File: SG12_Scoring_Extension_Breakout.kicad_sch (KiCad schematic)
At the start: 14 parts, among them J1 RJ45, J2 Barrel_Jack_MountingPin, J3 Barrel_Jack_MountingPin, J4 Barrel_Jack_MountingPin, J5 Barrel_Jack_MountingPin, J6 Barrel_Jack_MountingPin, Q1 IRF4905, Q2 IRF4905, Q3 IRF4905, Q4 IRF4905

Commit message: Messed up a footprint
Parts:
- R4: footprint Connector_RJ:RJ45_Amphenol_54602-x08_Horizontal -> Resistor_THT:R_Axial_DIN0207_L6.3mm_D2.5mm_P10.16mm_Horizontal
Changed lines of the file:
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@@
       (effects (font (size 1.27 1.27)) (justify left))
     )
-    (property "Footprint" "Connector_RJ:RJ45_Amphenol_54602-x08_Horizontal" (at 115.062 157.48 90)
+    (property "Footprint" "Resistor_THT:R_Axial_DIN0207_L6.3mm_D2.5mm_P10.16mm_Horizontal" (at 115.062 157.48 90)
       (effects (font (size 1.27 1.27)) hide)
     )

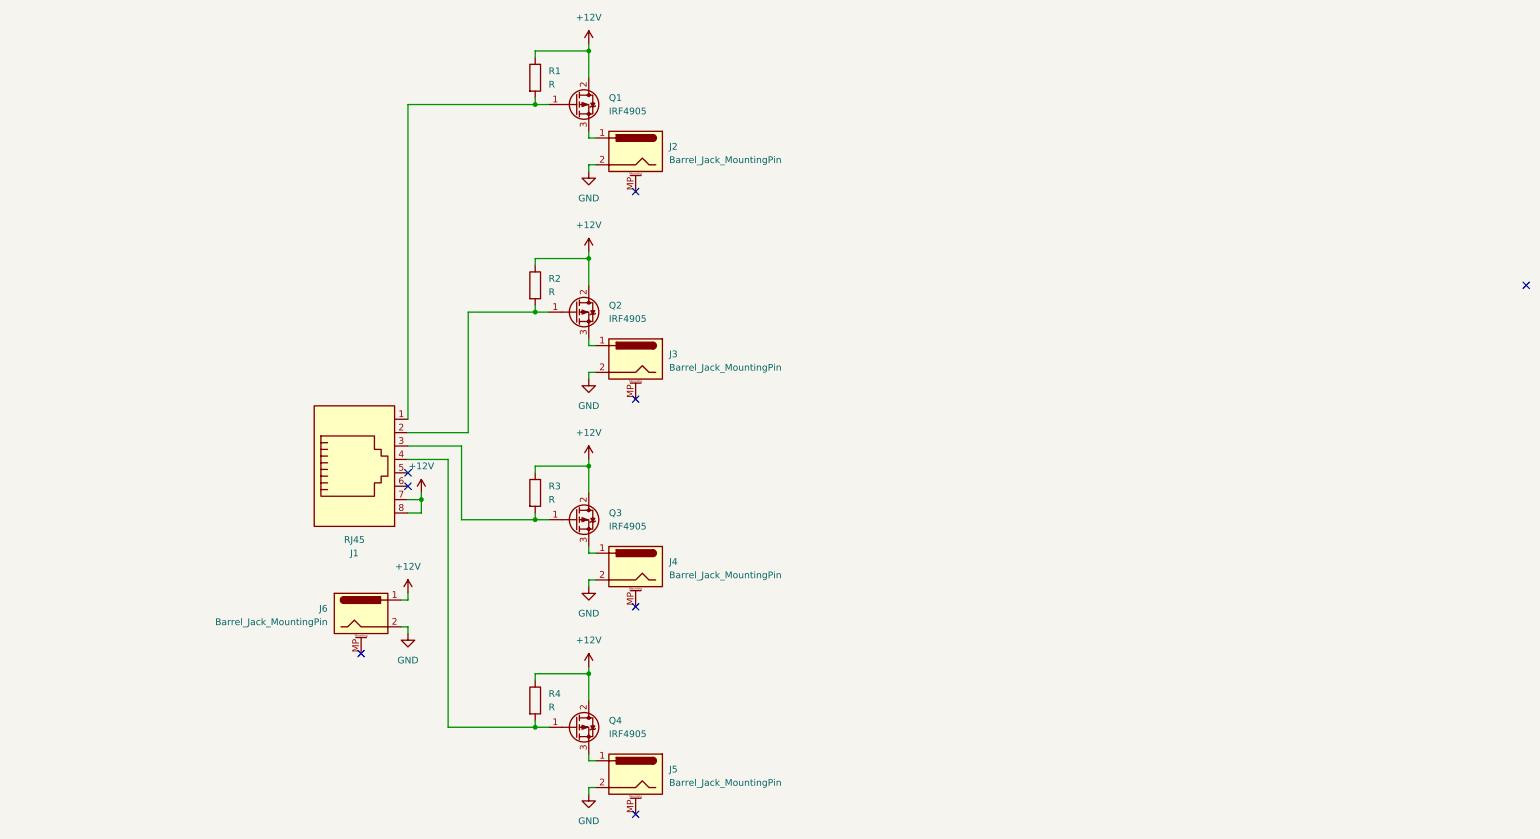
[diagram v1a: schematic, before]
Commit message: Added decoupling capacitors and extra header
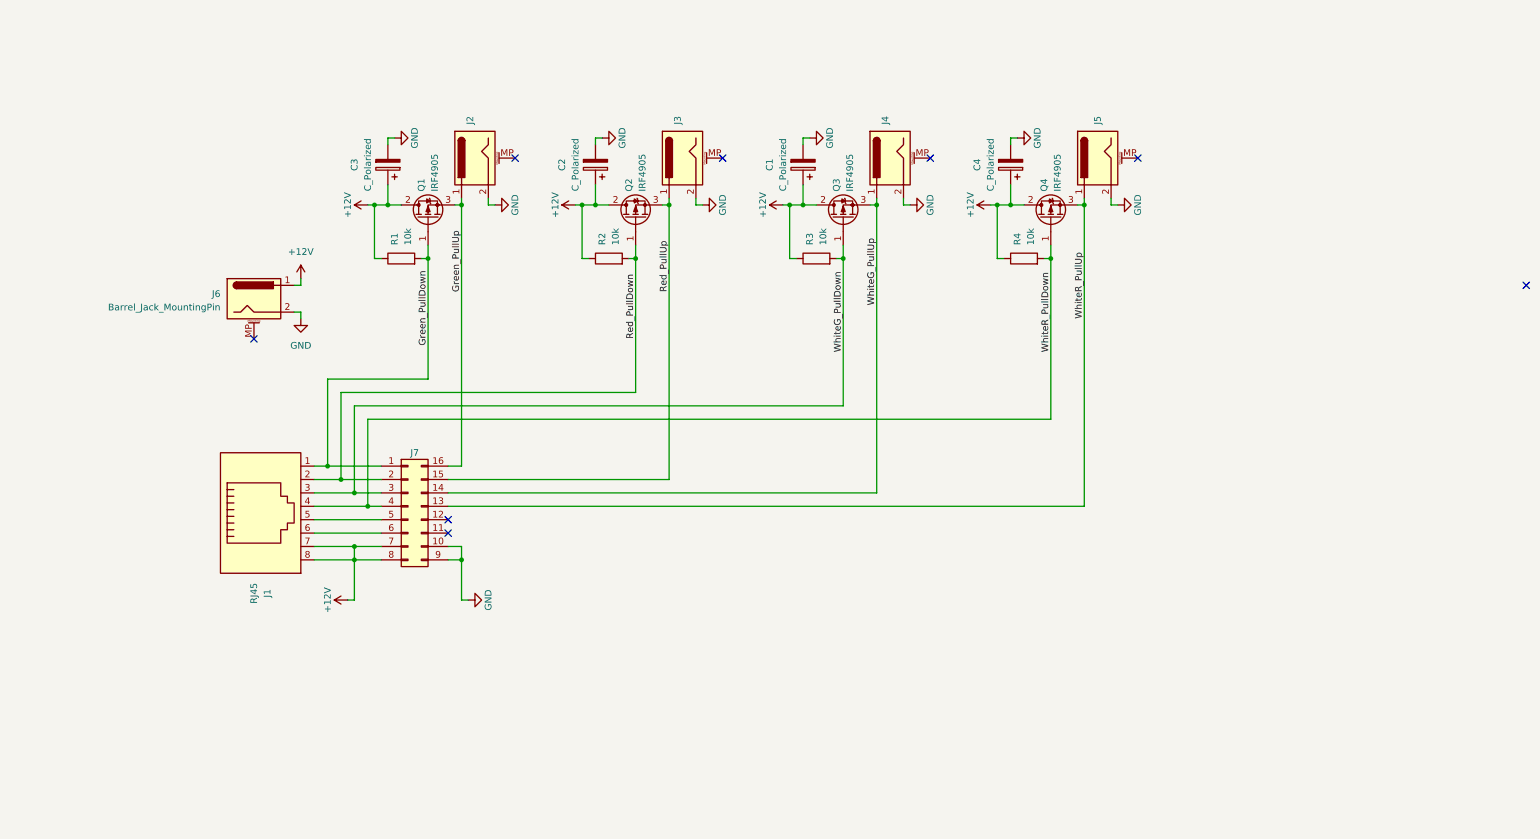
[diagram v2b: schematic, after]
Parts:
- added C1, C2, C3, C4: C_Polarized, symbol Device:C_Polarized
- added J7: Conn_02x08_Counter_Clockwise, symbol Connector_Generic:Conn_02x08_Counter_Clockwise
- R1, R2, R3, R4: value R -> 10k
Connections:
- net +12V: now also C1.1, C2.1, C3.1, C4.1, J7.7 (Pin_7), J7.8 (Pin_8)
- net GND: now also C1.2, C2.2, C3.2, C4.2, J7.10 (Pin_10), J7.9 (Pin_9)
- net Red_PullUp: now reaches J3.1, Q2.3 (S)
- net Red_PullUp: now also J7.15 (Pin_15)
- net WhiteR_PullDown: now reaches J1.4, Q4.1 (G), R4.2
- net WhiteR_PullDown: now also J7.4 (Pin_4)
- net WhiteR_PullUp: now reaches J5.1, Q4.3 (S)
- net WhiteR_PullUp: now also J7.13 (Pin_13)
- net WhiteG_PullDown: now reaches J1.3, Q3.1 (G), R3.2
- net WhiteG_PullDown: now also J7.3 (Pin_3)
- net WhiteG_PullUp: now reaches J4.1, Q3.3 (S)
- net WhiteG_PullUp: now also J7.14 (Pin_14)
- net Green_PullDown: now reaches J1.1, Q1.1 (G), R1.2
- net Green_PullDown: now also J7.1 (Pin_1)
- net Red_PullDown: now reaches J1.2, Q2.1 (G), R2.2
- net Red_PullDown: now also J7.2 (Pin_2)
- net Green_PullUp: now reaches J2.1, Q1.3 (S)
- net Green_PullUp: now also J7.16 (Pin_16)
- net at J1.5: now also J7.5 (Pin_5)
- net at J1.6: now also J7.6 (Pin_6)
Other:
- moved on the sheet: J1, J2, J3, J4, J5, J6, Q1, Q2, Q3, Q4, R1, R2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

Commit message: Added footprints
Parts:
- C1, C2, C3, C4: footprint (none) -> Capacitor_THT:CP_Radial_D6.3mm_P2.50mm
- J7: footprint (none) -> Connector_PinHeader_2.54mm:PinHeader_2x08_P2.54mm_Vertical
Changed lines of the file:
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@@
       (effects (font (size 1.27 1.27)))
     )
-    (property "Footprint" "" (at 87.9348 52.07 0)
+    (property "Footprint" "Capacitor_THT:CP_Radial_D6.3mm_P2.50mm" (at 87.9348 52.07 0)
       (effects (font (size 1.27 1.27)) hide)
     )
@@
       (effects (font (size 1.27 1.27)))
     )
-    (property "Footprint" "" (at 127.3048 52.07 0)
+    (property "Footprint" "Capacitor_THT:CP_Radial_D6.3mm_P2.50mm" (at 127.3048 52.07 0)
       (effects (font (size 1.27 1.27)) hide)
     )
@@
       (effects (font (size 1.27 1.27)) hide)
     )
-    (property "Footprint" "" (at 92.71 120.65 0)
+    (property "Footprint" "Connector_PinHeader_2.54mm:PinHeader_2x08_P2.54mm_Vertical" (at 92.71 120.65 0)
       (effects (font (size 1.27 1.27)) hide)
     )
@@
       (effects (font (size 1.27 1.27)))
     )
-    (property "Footprint" "" (at 166.6748 52.07 0)
+    (property "Footprint" "Capacitor_THT:CP_Radial_D6.3mm_P2.50mm" (at 166.6748 52.07 0)
       (effects (font (size 1.27 1.27)) hide)
     )
@@
       (effects (font (size 1.27 1.27)))
     )
-    (property "Footprint" "" (at 206.0448 52.07 0)
-      (effects (font (size 1.27 1.27)) hide)
-    )
+    (property "Footprint" "Capacitor_THT:CP_Radial_D6.3mm_P2.50mm" (at 206.0448 52.07 0)
+      (effects (font (size 1.27 1.27)) hide)
+    )

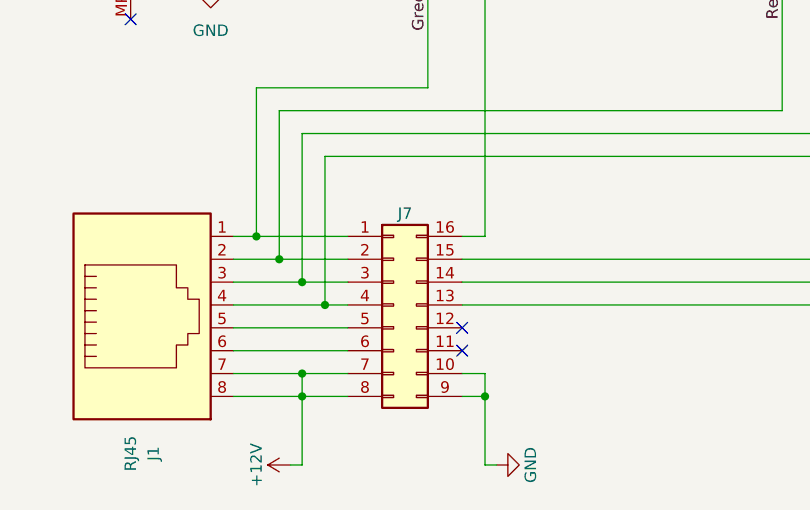
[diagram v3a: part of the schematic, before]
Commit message: Finished up initial routing, need to check rules
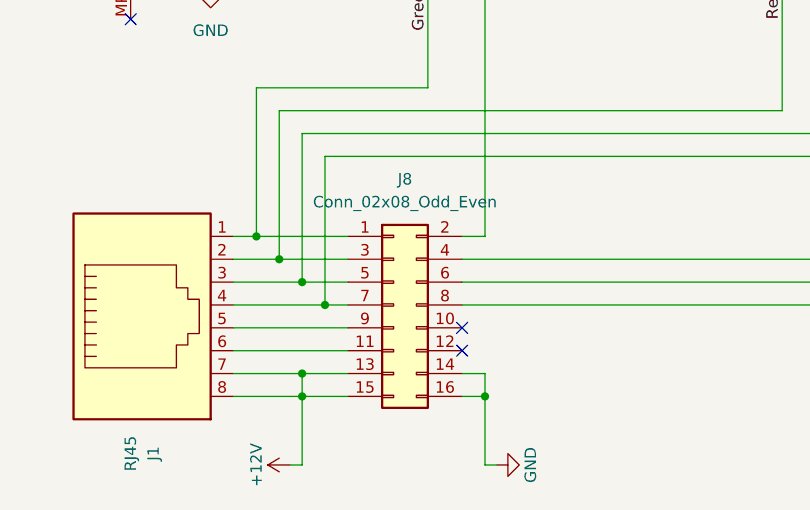
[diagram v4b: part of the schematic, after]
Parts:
- removed J7: Conn_02x08_Counter_Clockwise, Connector_PinHeader_2.54mm:PinHeader_2x08_P2.54mm_Vertical, symbol Connector_Generic:Conn_02x08_Counter_Clockwise
- added J8: Conn_02x08_Odd_Even, Connector_PinHeader_2.54mm:PinHeader_2x08_P2.54mm_Vertical, symbol Connector_Generic:Conn_02x08_Odd_Even
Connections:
- net +12V: now also J8.13 (Pin_13), J8.15 (Pin_15)
- net GND: now also J8.14 (Pin_14), J8.16 (Pin_16)
- net Green_PullDown: now also J8.1 (Pin_1)
- net Green_PullUp: now also J8.2 (Pin_2)
- net Red_PullDown: now also J8.3 (Pin_3)
- net Red_PullUp: now also J8.4 (Pin_4)
- net WhiteG_PullDown: now also J8.5 (Pin_5)
- net WhiteG_PullUp: now also J8.6 (Pin_6)
- net WhiteR_PullDown: now also J8.7 (Pin_7)
- net WhiteR_PullUp: now also J8.8 (Pin_8)
- net at J1.5: now also J8.9 (Pin_9)
- net at J1.6: now also J8.11 (Pin_11)
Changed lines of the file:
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@@
     )
   )
-  (symbol (lib_id "power:GND") (at 90.17 50.8 90) (unit 1)
-    (in_bom yes) (on_board yes) (dnp no)
-    (property "Reference" "#PWR015" (at 96.52 50.8 0)
-      (effects (font (size 1.27 1.27)) hide)
-    )
-    (property "Value" "GND" (at 93.98 50.8 0)
+  (symbol (lib_id "Connector_Generic:Conn_02x08_Odd_Even") (at 92.71 120.65 0) (unit 1)
+    (in_bom yes) (on_board yes) (dnp no) (fields_autoplaced)
+    (property "Reference" "J8" (at 93.98 106.68 0)
       (effects (font (size 1.27 1.27)))
     )
-    (property "Footprint" "" (at 90.17 50.8 0)
-      (effects (font (size 1.27 1.27)) hide)
-    )
-    (property "Datasheet" "" (at 90.17 50.8 0)
-      (effects (font (size 1.27 1.27)) hide)
-    )
-    (pin "1")
-    (instances
-      (project "SG12_Scoring_Extension_Breakout"
-        (path "/d3a18a1f-0030-40cf-934c-0abb5a098964"
-          (reference "#PWR015") (unit 1)
-        )
-      )
-    )
-  )
-  (symbol (lib_id "Connector_Generic:Conn_02x08_Counter_Clockwise") (at 92.71 120.65 0) (unit 1)
-    (in_bom yes) (on_board yes) (dnp no)
-    (property "Reference" "J7" (at 93.98 110.49 0)
+    (property "Value" "Conn_02x08_Odd_Even" (at 93.98 109.22 0)
       (effects (font (size 1.27 1.27)))
-    )
-    (property "Value" "Conn_02x08_Counter_Clockwise" (at 93.98 109.22 0)
-      (effects (font (size 1.27 1.27)) hide)
     )
     (property "Footprint" "Connector_PinHeader_2.54mm:PinHeader_2x08_P2.54mm_Vertical" (at 92.71 120.65 0)
@@
       (project "SG12_Scoring_Extension_Breakout"
         (path "/d3a18a1f-0030-40cf-934c-0abb5a098964"
-          (reference "J7") (unit 1)
+          (reference "J8") (unit 1)
         )
       )
+    )
+  )
+  (symbol (lib_id "power:GND") (at 90.17 50.8 90) (unit 1)
+    (in_bom yes) (on_board yes) (dnp no)
+    (property "Reference" "#PWR015" (at 96.52 50.8 0)
+      (effects (font (size 1.27 1.27)) hide)
+    )
+    (property "Value" "GND" (at 93.98 50.8 0)
+      (effects (font (size 1.27 1.27)))
+    )
+    (property "Footprint" "" (at 90.17 50.8 0)
+      (effects (font (size 1.27 1.27)) hide)
+    )
+    (property "Datasheet" "" (at 90.17 50.8 0)
+      (effects (font (size 1.27 1.27)) hide)
+    )
+    (pin "1")
+    (instances
+      (project "SG12_Scoring_Extension_Breakout"
+        (path "/d3a18a1f-0030-40cf-934c-0abb5a098964"
+          (reference "#PWR015") (unit 1)
+        )
+      )

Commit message: Updated routing and RJ45 footprint
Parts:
- J1: footprint Connector_RJ:RJ45_Amphenol_54602-x08_Horizontal -> Connector_RJ:RJ45_Ninigi_GE
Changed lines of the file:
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@@
       (effects (font (size 1.27 1.27)))
     )
-    (property "Footprint" "Connector_RJ:RJ45_Amphenol_54602-x08_Horizontal" (at 64.77 121.285 90)
+    (property "Footprint" "Connector_RJ:RJ45_Ninigi_GE" (at 64.77 121.285 90)
       (effects (font (size 1.27 1.27)) hide)
     )

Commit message: Added 3d models for barrel jacks
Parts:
- J1: footprint Connector_RJ:RJ45_Ninigi_GE -> Connector_RJ:RJ45_Amphenol_54602-x08_Horizontal
- J2, J3, J4, J5, J6: footprint Connector_BarrelJack:BarrelJack_GCT_DCJ200-10-A_Horizontal -> Library:BarrelJack_GCT_DCJ200-10-A_Horizontal
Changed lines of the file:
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@@
       (effects (font (size 1.27 1.27)) (justify right))
     )
-    (property "Footprint" "Connector_BarrelJack:BarrelJack_GCT_DCJ200-10-A_Horizontal" (at 64.77 82.296 0)
+    (property "Footprint" "Library:BarrelJack_GCT_DCJ200-10-A_Horizontal" (at 64.77 82.296 0)
       (effects (font (size 1.27 1.27)) hide)
     )
@@
       (effects (font (size 1.27 1.27)) (justify right) hide)
     )
-    (property "Footprint" "Connector_BarrelJack:BarrelJack_GCT_DCJ200-10-A_Horizontal" (at 145.796 55.88 0)
+    (property "Footprint" "Library:BarrelJack_GCT_DCJ200-10-A_Horizontal" (at 145.796 55.88 0)
       (effects (font (size 1.27 1.27)) hide)
     )
@@
       (effects (font (size 1.27 1.27)) (justify right) hide)
     )
-    (property "Footprint" "Connector_BarrelJack:BarrelJack_GCT_DCJ200-10-A_Horizontal" (at 224.536 55.88 0)
+    (property "Footprint" "Library:BarrelJack_GCT_DCJ200-10-A_Horizontal" (at 224.536 55.88 0)
       (effects (font (size 1.27 1.27)) hide)
     )
@@
       (effects (font (size 1.27 1.27)) (justify right) hide)
     )
-    (property "Footprint" "Connector_BarrelJack:BarrelJack_GCT_DCJ200-10-A_Horizontal" (at 185.166 55.88 0)
+    (property "Footprint" "Library:BarrelJack_GCT_DCJ200-10-A_Horizontal" (at 185.166 55.88 0)
       (effects (font (size 1.27 1.27)) hide)
     )
@@
       (effects (font (size 1.27 1.27)) (justify right) hide)
     )
-    (property "Footprint" "Connector_BarrelJack:BarrelJack_GCT_DCJ200-10-A_Horizontal" (at 106.426 55.88 0)
+    (property "Footprint" "Library:BarrelJack_GCT_DCJ200-10-A_Horizontal" (at 106.426 55.88 0)
       (effects (font (size 1.27 1.27)) hide)
     )
@@
       (effects (font (size 1.27 1.27)))
     )
-    (property "Footprint" "Connector_RJ:RJ45_Ninigi_GE" (at 64.77 121.285 90)
-      (effects (font (size 1.27 1.27)) hide)
-    )
+    (property "Footprint" "Connector_RJ:RJ45_Amphenol_54602-x08_Horizontal" (at 64.77 121.285 90)
+      (effects (font (size 1.27 1.27)) hide)
+    )
